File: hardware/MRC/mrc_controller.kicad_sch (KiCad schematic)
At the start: 72 parts, among them J10 Conn_02x04_Odd_Even, J11 Conn_02x07_Odd_Even, J15 RJ45_Wuerth_7499010121A, J23 USB_B_Mini, J24 Micro_SD_Card_Det_Hirose_DM3AT, U13 LAN8742A, U17 USBLC6-4SC6, U9 STM32F767ZITx, X1 50M, Y1 X53T-C20SSA-25.000MHz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

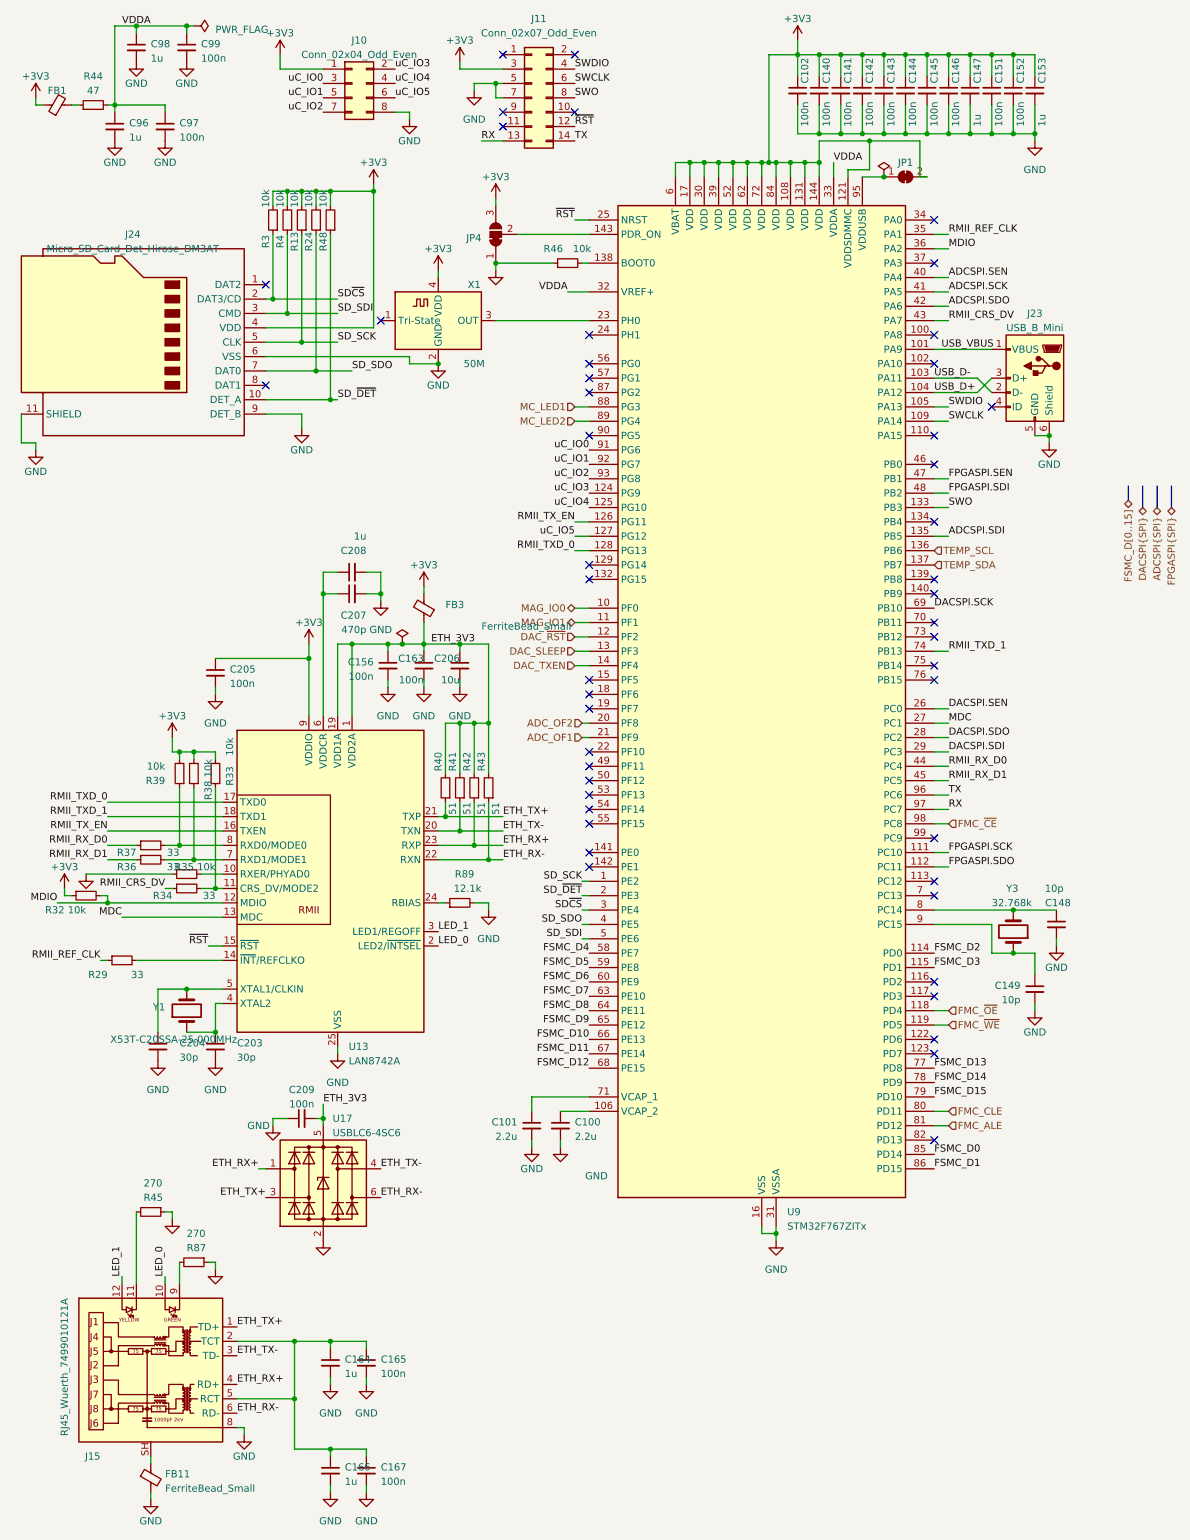
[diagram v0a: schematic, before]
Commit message: Update KiCAD Version, Integrate Libraries
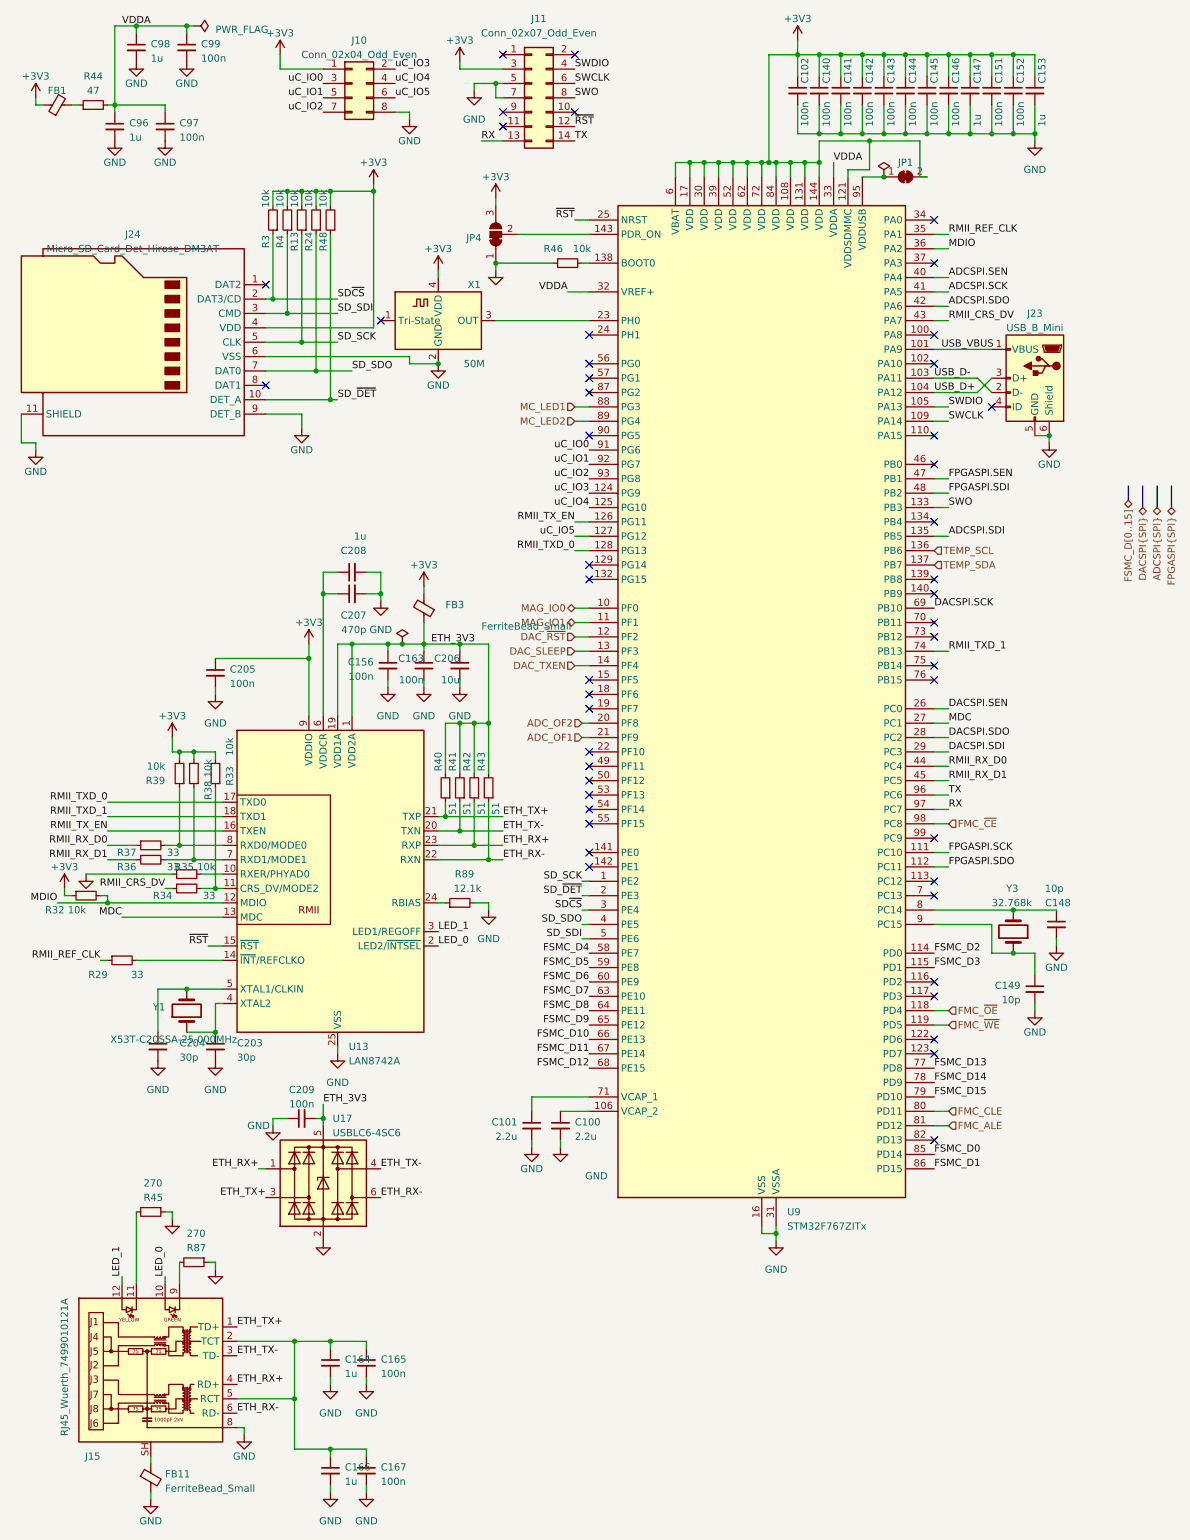
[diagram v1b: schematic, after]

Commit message: Clean bill of materials
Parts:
- C100, C101: MPN (none) -> KGM15BR50J225KT
- C102, C140, C141, C142, C143, C144, C145, C146, C151, C152, C156, C163, C165, C167, C205, C209, C97, C99: MPN (none) -> C0603C104K1RACAUTO
- C147, C153, C164, C166, C208, C96, C98: MPN (none) -> KGM15BR51E105KM
- C148, C149: MPN (none) -> KGM15ACG2A100FT
- C203, C204: MPN (none) -> C0603C300J5G
- C206: MPN (none) -> KGM21AR50J106KU
- C207: MPN (none) -> KGM15AR71H471KT
- FB1, FB11, FB3: MPN (none) -> 742792641
- J11: MPN (none) -> FTSH10701FDVKP
- J15: MPN (none) -> 7499010121A
- J23: MPN (none) -> 65100516121
- J24: MPN (none) -> DM3BT-DSF-PEJS
- R13, R24, R3, R32, R33, R35, R38, R39, R4, R46, R48: MPN (none) -> CMP0603AFX-1002L
- R29, R34, R36, R37: MPN (none) -> SDR03EZPF33R0
- R40, R41, R42, R43: MPN (none) -> SDR03EZPF51R0
- R44: MPN (none) -> SDR03EZPF47R0
- R45, R87: MPN (none) -> ERJ-3GEYJ271V
- R89: MPN (none) -> KTR03EZPF1212
- U13: MPN (none) -> LAN8742AI-CZ-TR
- U17: MPN (none) -> USBLC6-4SC6
- U9: MPN (none) -> STM32F767ZIT6
- X1: MPN (none) -> 2520MV-500-DN-TR
- Y3: MPN (none) -> 202257-MC01
